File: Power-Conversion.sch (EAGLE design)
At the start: 40 parts, among them Q1 SUM90P10-19L, U7 LM2678

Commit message: Started Board Layout
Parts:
- removed U$2: SAMTEC-10, SAMTEC-10:SAMTEC-10
- added U$16: POWER_BRICK_CONNECTORS(2X6), MotherBoardParts2:POWER_BRICK_CONNECTORS(2X6)
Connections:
- net 12V: now also U$16.P$1, U$16.P$2, U$16.P$3; no longer U$2.P$1, U$2.P$2, U$2.P$3
- net 48_I_ANALOG: now also U$16.P$5
- net GND: now also U$16.P$7, U$16.P$8, U$16.P$9; no longer U$2.P$6, U$2.P$7, U$2.P$8
- net SCL: now also U$16.P$12; no longer U$2.P$5
- net SDA: now also U$16.P$6; no longer U$2.P$10
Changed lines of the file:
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@@
 <?xml version="1.0" encoding="utf-8"?>
 <!DOCTYPE eagle SYSTEM "eagle.dtd">
-<eagle version="8.3.2">
+<eagle version="8.4.1">
 <drawing>
 <settings>
@@
 <part name="SUPPLY1" library="SparkFun-PowerSymbols" deviceset="12V" device=""/>
 <part name="SUPPLY2" library="SparkFun-PowerSymbols" deviceset="12V" device=""/>
-<part name="U$2" library="SAMTEC-10" deviceset="SAMTEC-10" device=""/>
-<part name="GND5" library="supply1" deviceset="GND" device=""/>
-<part name="SUPPLY3" library="SparkFun-PowerSymbols" deviceset="12V" device=""/>
 <part name="U$17" library="MotherBoardParts2" deviceset="POWER_BRICK_CONNECTORS(2X15)" device=""/>
 <part name="U$11" library="MotherBoardParts2" deviceset="POWER_BRICK_CONNECTORS(2X15)" device=""/>
@@
 <part name="P+8" library="supply1" library_urn="urn:adsk.eagle:library:371" deviceset="VCC" device=""/>
 <part name="P+9" library="supply1" library_urn="urn:adsk.eagle:library:371" deviceset="VCC" device=""/>
+<part name="U$16" library="MotherBoardParts2" deviceset="POWER_BRICK_CONNECTORS(2X6)" device=""/>
+<part name="GND6" library="supply1" deviceset="GND" device=""/>
+<part name="SUPPLY5" library="SparkFun-PowerSymbols" deviceset="12V" device=""/>
 </parts>
 <sheets>
@@
 <instance part="SUPPLY1" gate="G$1" x="78.74" y="434.34"/>
 <instance part="SUPPLY2" gate="G$1" x="78.74" y="477.52"/>
-<instance part="U$2" gate="G$1" x="50.8" y="505.46"/>
-<instance part="GND5" gate="1" x="83.82" y="502.92"/>
-<instance part="SUPPLY3" gate="G$1" x="17.78" y="515.62"/>
 <instance part="U$17" gate="G$1" x="185.42" y="472.44"/>
 <instance part="U$11" gate="G$1" x="261.62" y="472.44"/>
@@
 <instance part="P+8" gate="VCC" x="215.9" y="391.16"/>
 <instance part="P+9" gate="VCC" x="307.34" y="391.16"/>
+<instance part="U$16" gate="G$1" x="53.34" y="508"/>
+<instance part="GND6" gate="1" x="76.2" y="502.92"/>
+<instance part="SUPPLY5" gate="G$1" x="30.48" y="515.62"/>
 </instances>
 <busses>
@@
 </segment>
 <segment>
-<pinref part="U$2" gate="G$1" pin="P$6"/>
-<wire x1="66.04" y1="515.62" x2="76.2" y2="515.62" width="0.1524" layer="91"/>
-<wire x1="76.2" y1="515.62" x2="76.2" y2="510.54" width="0.1524" layer="91"/>
-<pinref part="U$2" gate="G$1" pin="P$7"/>
-<wire x1="76.2" y1="510.54" x2="66.04" y2="510.54" width="0.1524" layer="91"/>
-<pinref part="U$2" gate="G$1" pin="P$8"/>
-<wire x1="66.04" y1="505.46" x2="76.2" y2="505.46" width="0.1524" layer="91"/>
-<wire x1="76.2" y1="505.46" x2="76.2" y2="510.54" width="0.1524" layer="91"/>
-<junction x="76.2" y="510.54"/>
-<pinref part="GND5" gate="1" pin="GND"/>
-<wire x1="76.2" y1="510.54" x2="83.82" y2="510.54" width="0.1524" layer="91"/>
-<wire x1="83.82" y1="510.54" x2="83.82" y2="505.46" width="0.1524" layer="91"/>
-</segment>
-<segment>
 <pinref part="U$8" gate="G$1" pin="P$2"/>
 <pinref part="GND4" gate="1" pin="GND"/>
@@
 <pinref part="GND9" gate="1" pin="GND"/>
 </segment>
+<segment>
+<pinref part="U$16" gate="G$1" pin="P$7"/>
+<wire x1="66.04" y1="515.62" x2="71.12" y2="515.62" width="0.1524" layer="91"/>
+<wire x1="71.12" y1="515.62" x2="71.12" y2="510.54" width="0.1524" layer="91"/>
+<pinref part="U$16" gate="G$1" pin="P$8"/>
+<wire x1="71.12" y1="510.54" x2="66.04" y2="510.54" width="0.1524" layer="91"/>
+<pinref part="U$16" gate="G$1" pin="P$9"/>
+<wire x1="66.04" y1="505.46" x2="71.12" y2="505.46" width="0.1524" layer="91"/>
+<wire x1="71.12" y1="505.46" x2="71.12" y2="510.54" width="0.1524" layer="91"/>
+<junction x="71.12" y="510.54"/>
+<wire x1="71.12" y1="510.54" x2="76.2" y2="510.54" width="0.1524" layer="91"/>
+<wire x1="76.2" y1="510.54" x2="76.2" y2="505.46" width="0.1524" layer="91"/>
+<pinref part="GND6" gate="1" pin="GND"/>
+</segment>
 </net>
 <net name="ONOFF" class="0">
@@
 <net name="12V" class="0">
 <segment>
-<pinref part="U$2" gate="G$1" pin="P$1"/>
-<wire x1="35.56" y1="515.62" x2="25.4" y2="515.62" width="0.1524" layer="91"/>
-<pinref part="U$2" gate="G$1" pin="P$2"/>
-<wire x1="35.56" y1="510.54" x2="25.4" y2="510.54" width="0.1524" layer="91"/>
-<wire x1="25.4" y1="510.54" x2="25.4" y2="515.62" width="0.1524" layer="91"/>
-<pinref part="U$2" gate="G$1" pin="P$3"/>
-<wire x1="35.56" y1="505.46" x2="25.4" y2="505.46" width="0.1524" layer="91"/>
-<wire x1="25.4" y1="505.46" x2="25.4" y2="510.54" width="0.1524" layer="91"/>
-<junction x="25.4" y="510.54"/>
-<label x="25.4" y="515.62" size="1.778" layer="95"/>
-<pinref part="SUPPLY3" gate="G$1" pin="12V"/>
-<wire x1="25.4" y1="510.54" x2="17.78" y2="510.54" width="0.1524" layer="91"/>
-<wire x1="17.78" y1="510.54" x2="17.78" y2="515.62" width="0.1524" layer="91"/>
-</segment>
-<segment>
 <pinref part="U$8" gate="G$1" pin="P$1"/>
 <pinref part="SUPPLY2" gate="G$1" pin="12V"/>
@@
 <wire x1="78.74" y1="426.72" x2="78.74" y2="434.34" width="0.1524" layer="91"/>
 </segment>
+<segment>
+<pinref part="U$16" gate="G$1" pin="P$1"/>
+<wire x1="40.64" y1="515.62" x2="35.56" y2="515.62" width="0.1524" layer="91"/>
+<pinref part="U$16" gate="G$1" pin="P$2"/>
+<wire x1="35.56" y1="515.62" x2="35.56" y2="510.54" width="0.1524" layer="91"/>
+<wire x1="35.56" y1="510.54" x2="40.64" y2="510.54" width="0.1524" layer="91"/>
+<pinref part="U$16" gate="G$1" pin="P$3"/>
+<wire x1="40.64" y1="505.46" x2="35.56" y2="505.46" width="0.1524" layer="91"/>
+<wire x1="35.56" y1="505.46" x2="35.56" y2="510.54" width="0.1524" layer="91"/>
+<junction x="35.56" y="510.54"/>
+<wire x1="35.56" y1="510.54" x2="30.48" y2="510.54" width="0.1524" layer="91"/>
+<wire x1="30.48" y1="510.54" x2="30.48" y2="515.62" width="0.1524" layer="91"/>
+<pinref part="SUPPLY5" gate="G$1" pin="12V"/>
+</segment>
 </net>
 <net name="SCL" class="0">
-<segment>
-<pinref part="U$2" gate="G$1" pin="P$5"/>
-<wire x1="35.56" y1="495.3" x2="25.4" y2="495.3" width="0.1524" layer="91"/>
-<label x="25.4" y="495.3" size="1.778" layer="95"/>
-</segment>
 <segment>
 <pinref part="U$13" gate="G$1" pin="P$12"/>
@@
 <label x="342.9" y="345.44" size="1.778" layer="95"/>
 </segment>
+<segment>
+<pinref part="U$16" gate="G$1" pin="P$12"/>
+<wire x1="66.04" y1="490.22" x2="76.2" y2="490.22" width="0.1524" layer="91"/>
+<label x="71.12" y="490.22" size="1.778" layer="95"/>
+</segment>
 </net>
 <net name="SDA" class="0">
-<segment>
-<pinref part="U$2" gate="G$1" pin="P$10"/>
-<wire x1="66.04" y1="495.3" x2="76.2" y2="495.3" width="0.1524" layer="91"/>
-<label x="71.12" y="495.3" size="1.778" layer="95"/>
-</segment>
 <segment>
 <pinref part="U$13" gate="G$1" pin="P$6"/>
@@
 <wire x1="312.42" y1="345.44" x2="304.8" y2="345.44" width="0.1524" layer="91"/>
 <label x="304.8" y="345.44" size="1.778" layer="95"/>
+</segment>
+<segment>
+<pinref part="U$16" gate="G$1" pin="P$6"/>
+<wire x1="40.64" y1="490.22" x2="30.48" y2="490.22" width="0.1524" layer="91"/>
+<label x="30.48" y="490.22" size="1.778" layer="95"/>
 </segment>
 </net>
@@
 <label x="175.26" y="111.76" size="1.778" layer="95"/>
 </segment>
-</net>
+<segment>
+<pinref part="U$16" gate="G$1" pin="P$5"/>
+<wire x1="40.64" y1="495.3" x2="22.86" y2="495.3" width="0.1524" layer="91"/>
+<label x="22.86" y="495.3" size="1.778" layer="95"/>
+</segment>
+</net>

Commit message: Fix Board Layout
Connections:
- removed net +48_RAW: J1.1
- removed net 48_GND: J2.1
- net +48V_RAW: now also J1.1
- net 48V_GND: now also J2.1
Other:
- moved on the sheet: R3
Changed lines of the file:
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@@
 <instance part="P+3" gate="1" x="228.6" y="187.96"/>
 <instance part="P+4" gate="1" x="238.76" y="187.96"/>
-<instance part="R3" gate="G$1" x="119.38" y="175.26" rot="R90">
-<attribute name="PARTNO" value="1.00MHCT-ND" x="119.38" y="175.26" size="0.0254" layer="96" font="vector" display="off"/>
-<attribute name="BOM" value="INCLUDE" x="119.38" y="175.26" size="0.0254" layer="96" font="vector" display="off"/>
+<instance part="R3" gate="G$1" x="119.38" y="172.72" rot="R90">
+<attribute name="PARTNO" value="1.00MHCT-ND" x="119.38" y="172.72" size="0.0254" layer="96" font="vector" display="off"/>
+<attribute name="BOM" value="INCLUDE" x="119.38" y="172.72" size="0.0254" layer="96" font="vector" display="off"/>
 </instance>
 <instance part="D1" gate="G$1" x="129.54" y="187.96" smashed="yes" rot="R90">
@@
 <segment>
 <pinref part="R3" gate="G$1" pin="1"/>
-<wire x1="119.38" y1="170.18" x2="119.38" y2="157.48" width="0.1524" layer="91"/>
+<wire x1="119.38" y1="167.64" x2="119.38" y2="157.48" width="0.1524" layer="91"/>
 <label x="119.38" y="157.48" size="1.778" layer="95"/>
 </segment>
@@
 <pinref part="P-6" gate="1" pin="V-"/>
 <label x="292.1" y="360.68" size="1.778" layer="95"/>
+</segment>
+<segment>
+<pinref part="J2" gate="G$1" pin="1"/>
+<wire x1="30.48" y1="99.06" x2="20.32" y2="99.06" width="0.1524" layer="91"/>
+<label x="20.32" y="99.06" size="1.778" layer="95"/>
 </segment>
 </net>
@@
 <pinref part="R3" gate="G$1" pin="2"/>
 <pinref part="D1" gate="G$1" pin="A"/>
-<wire x1="119.38" y1="182.88" x2="119.38" y2="180.34" width="0.1524" layer="91"/>
+<wire x1="119.38" y1="182.88" x2="119.38" y2="177.8" width="0.1524" layer="91"/>
 <wire x1="129.54" y1="185.42" x2="129.54" y2="182.88" width="0.1524" layer="91"/>
 <wire x1="129.54" y1="182.88" x2="119.38" y2="182.88" width="0.1524" layer="91"/>
@@
 <wire x1="106.68" y1="203.2" x2="99.06" y2="203.2" width="0.1524" layer="91"/>
 <label x="99.06" y="203.2" size="1.778" layer="95"/>
+</segment>
+<segment>
+<pinref part="J1" gate="G$1" pin="1"/>
+<wire x1="30.48" y1="104.14" x2="20.32" y2="104.14" width="0.1524" layer="91"/>
+<label x="20.32" y="104.14" size="1.778" layer="95"/>
 </segment>
 </net>
@@
 </segment>
 </net>
-<net name="+48_RAW" class="0">
-<segment>
-<pinref part="J1" gate="G$1" pin="1"/>
-<wire x1="30.48" y1="104.14" x2="20.32" y2="104.14" width="0.1524" layer="91"/>
-<label x="20.32" y="104.14" size="1.778" layer="95"/>
-</segment>
-</net>
-<net name="48_GND" class="0">
-<segment>
-<pinref part="J2" gate="G$1" pin="1"/>
-<wire x1="30.48" y1="99.06" x2="20.32" y2="99.06" width="0.1524" layer="91"/>
-<label x="20.32" y="99.06" size="1.778" layer="95"/>
-</segment>
-</net>

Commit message: Routed Board
Added Diodes
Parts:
- added U$18, U$19, U$2: DIODE, diode:DIODE
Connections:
- removed net +48_SNS: U$1.IP-@3, U$1.IP-@4
- removed net VCC: U$13.P$1, U$13.P$2, U$13.P$7, U$13.P$8, U$14.P$1, U$14.P$2, U$14.P$7, U$14.P$8, U$15.P$1, U$15.P$2, U$15.P$7, U$15.P$8
- new net +12V_1: U$17.P$1, U$17.P$16, U$17.P$17, U$17.P$18, U$17.P$19, U$17.P$2, U$17.P$20, U$17.P$21, U$17.P$22, U$17.P$3, U$17.P$4, U$17.P$5, U$17.P$6, U$17.P$7, U$2.IN2
- new net +12V_2: U$11.P$1, U$11.P$16, U$11.P$17, U$11.P$18, U$11.P$19, U$11.P$2, U$11.P$20, U$11.P$21, U$11.P$22, U$11.P$3, U$11.P$4, U$11.P$5, U$11.P$6, U$11.P$7, U$18.IN2
- new net +12V_3: U$12.P$1, U$12.P$16, U$12.P$17, U$12.P$18, U$12.P$19, U$12.P$2, U$12.P$20, U$12.P$21, U$12.P$22, U$12.P$3, U$12.P$4, U$12.P$5, U$12.P$6, U$12.P$7, U$19.IN2
- new net +48V_SNS: U$1.IP-@3, U$1.IP-@4, U$13.P$1, U$13.P$2, U$13.P$7, U$13.P$8, U$14.P$1, U$14.P$2, U$14.P$7, U$14.P$8, U$15.P$1, U$15.P$2, U$15.P$7, U$15.P$8
- net +12V: now also U$18.OUT, U$19.OUT, U$2.OUT; no longer U$11.P$1, U$11.P$16, U$11.P$17, U$11.P$18, U$11.P$19, U$11.P$2, U$11.P$20, U$11.P$21, U$11.P$22, U$11.P$3, U$11.P$4, U$11.P$5, U$11.P$6, U$11.P$7, U$12.P$1, U$12.P$16, U$12.P$17, U$12.P$18, U$12.P$19, U$12.P$2, U$12.P$20, U$12.P$21, U$12.P$22, U$12.P$3, U$12.P$4, U$12.P$5, U$12.P$6, U$12.P$7, U$17.P$1, U$17.P$16, U$17.P$17, U$17.P$18, U$17.P$19, U$17.P$2, U$17.P$20, U$17.P$21, U$17.P$22, U$17.P$3, U$17.P$4, U$17.P$5, U$17.P$6, U$17.P$7
- net 12V: now also U$8.P$2; no longer U$3.P$2
- net GND: now also U$3.P$2; no longer U$8.P$2

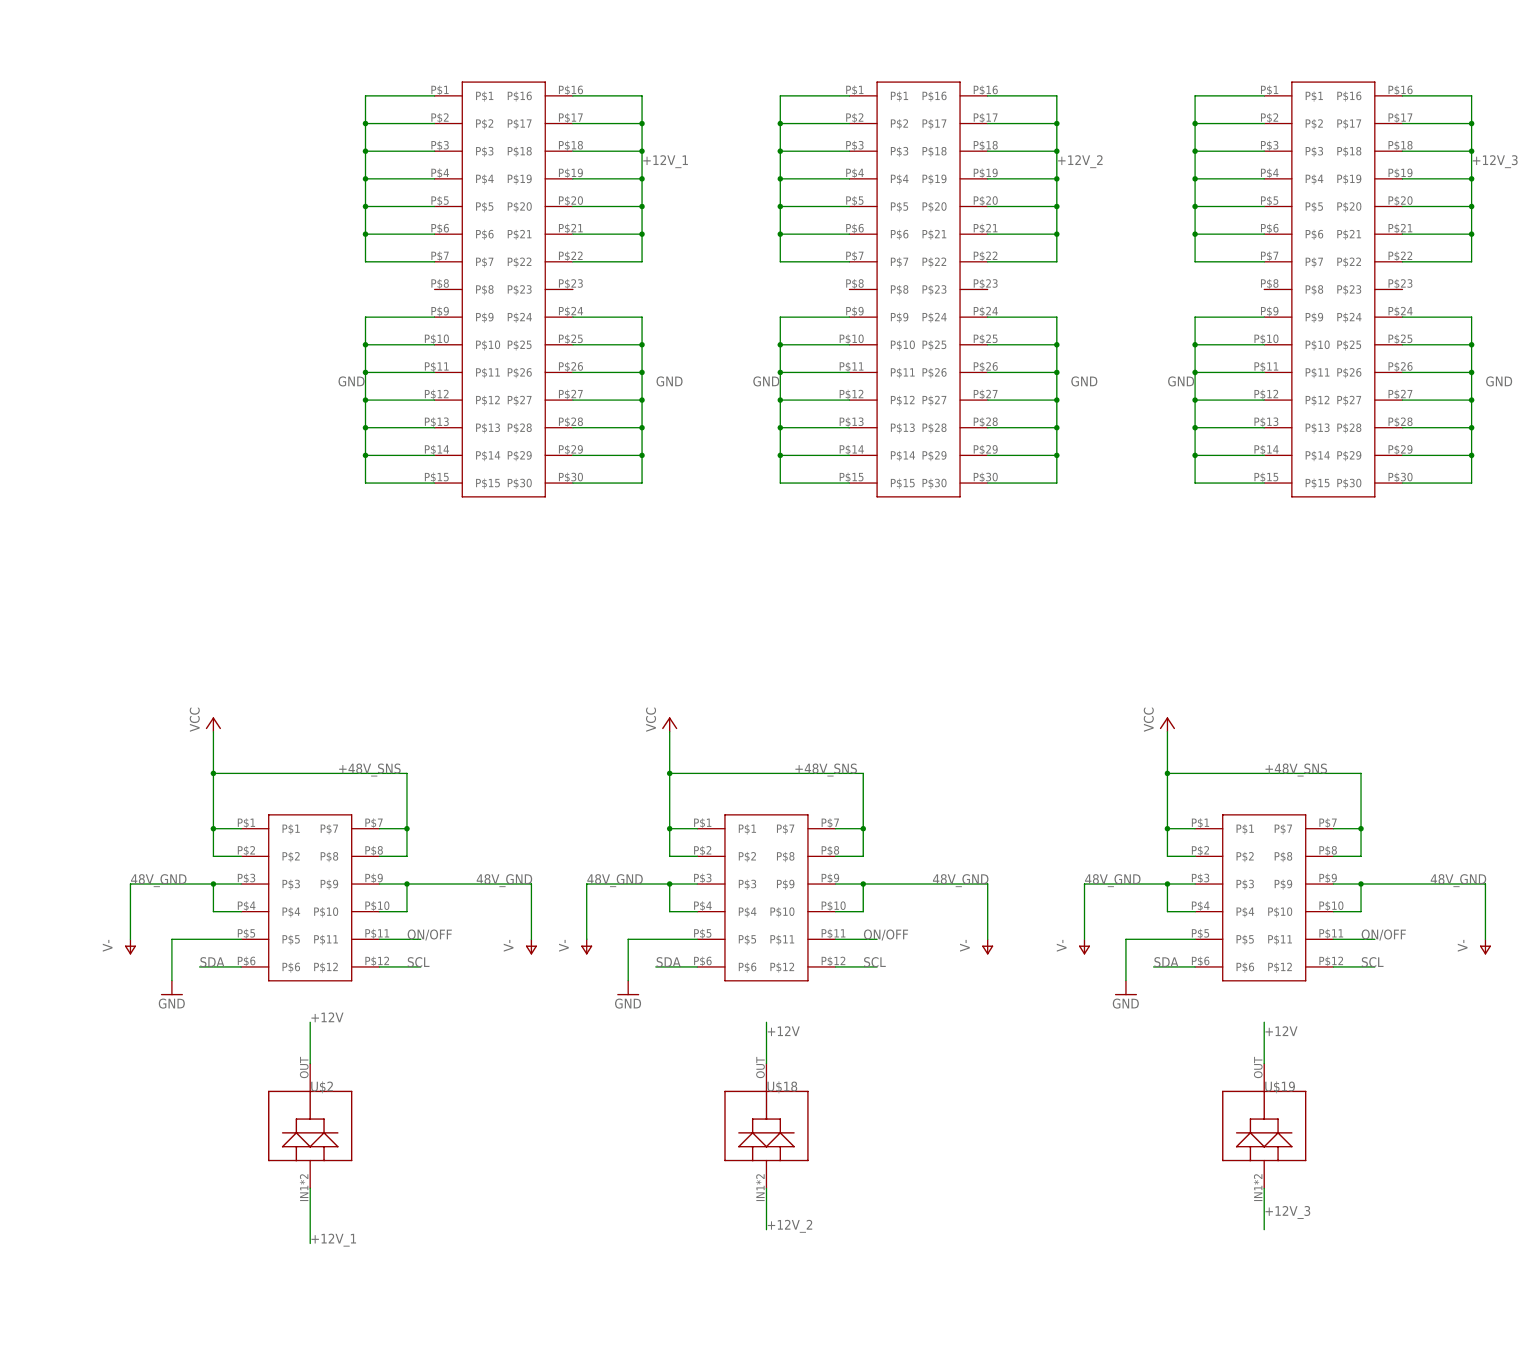
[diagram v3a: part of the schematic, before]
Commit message: Added new connectors for 8th bricks
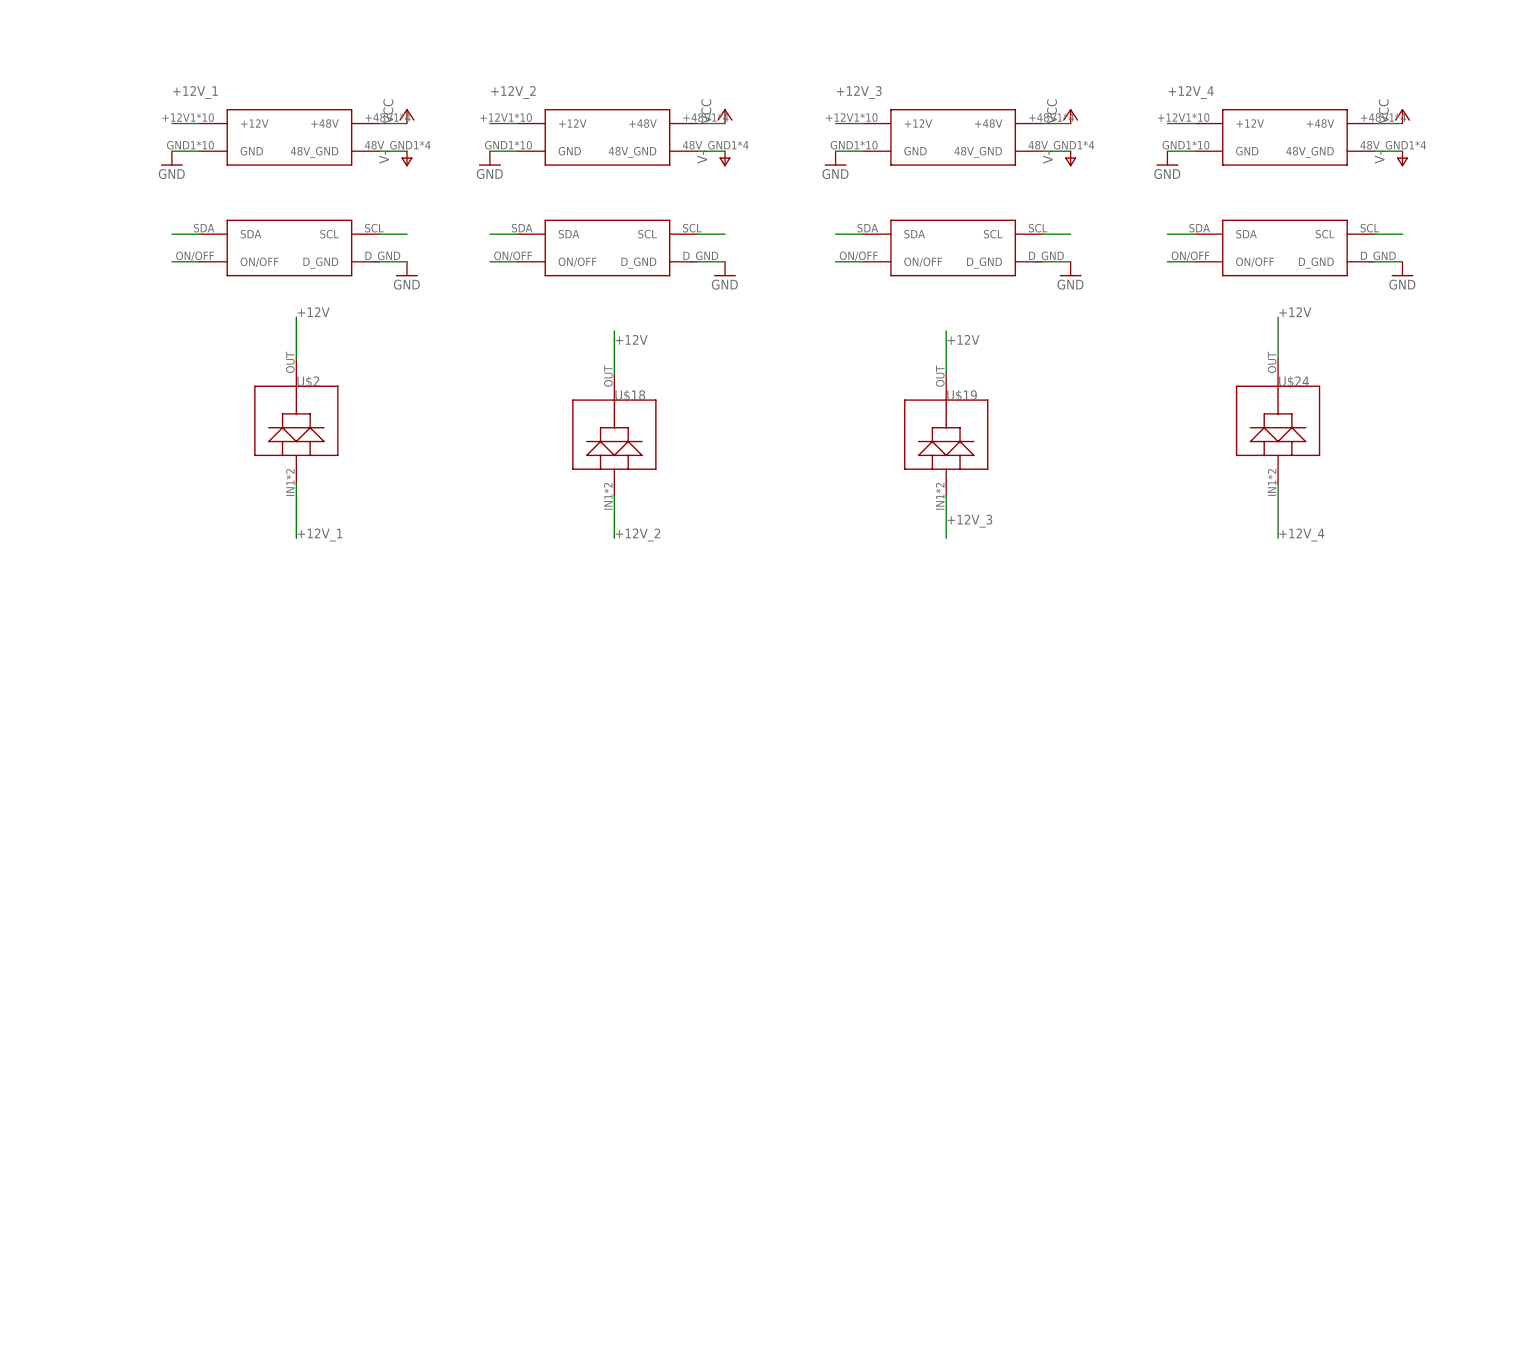
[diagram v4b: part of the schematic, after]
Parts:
- removed U$11, U$12, U$17: POWER_BRICK_CONNECTORS(2X15), MotherBoardParts2:POWER_BRICK_CONNECTORS(2X15)
- removed U$13, U$14, U$15: POWER_BRICK_CONNECTORS(2X6), MotherBoardParts2:POWER_BRICK_CONNECTORS(2X6)
- added U$20, U$21, U$22, U$23: BRICK_TO_POWER_DIST_WHOLE, MotherBoardParts2:BRICK_TO_POWER_DIST_WHOLE
- added U$24: DIODE, diode:DIODE
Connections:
- new net +12V_4: U$23.+12V, U$24.IN2
- new net V-: U$20.48V_GND, U$21.48V_GND, U$22.48V_GND, U$23.48V_GND
- new net VCC: U$20.+48V, U$21.+48V, U$22.+48V, U$23.+48V
- net +12V: now also U$24.OUT
- net +12V_1: now also U$20.+12V; no longer U$17.P$1, U$17.P$16, U$17.P$17, U$17.P$18, U$17.P$19, U$17.P$2, U$17.P$20, U$17.P$21, U$17.P$22, U$17.P$3, U$17.P$4, U$17.P$5, U$17.P$6, U$17.P$7
- net +12V_2: now also U$21.+12V; no longer U$11.P$1, U$11.P$16, U$11.P$17, U$11.P$18, U$11.P$19, U$11.P$2, U$11.P$20, U$11.P$21, U$11.P$22, U$11.P$3, U$11.P$4, U$11.P$5, U$11.P$6, U$11.P$7
- net +12V_3: now also U$22.+12V; no longer U$12.P$1, U$12.P$16, U$12.P$17, U$12.P$18, U$12.P$19, U$12.P$2, U$12.P$20, U$12.P$21, U$12.P$22, U$12.P$3, U$12.P$4, U$12.P$5, U$12.P$6, U$12.P$7
- net +48V_SNS: no longer U$13.P$1, U$13.P$2, U$13.P$7, U$13.P$8, U$14.P$1, U$14.P$2, U$14.P$7, U$14.P$8, U$15.P$1, U$15.P$2, U$15.P$7, U$15.P$8
- net 48V_GND: no longer U$13.P$10, U$13.P$3, U$13.P$4, U$13.P$9, U$14.P$10, U$14.P$3, U$14.P$4, U$14.P$9, U$15.P$10, U$15.P$3, U$15.P$4, U$15.P$9
- net GND: now also U$20.D_GND, U$20.GND, U$21.D_GND, U$21.GND, U$22.D_GND, U$22.GND, U$23.D_GND, U$23.GND; no longer U$11.P$10, U$11.P$11, U$11.P$12, U$11.P$13, U$11.P$14, U$11.P$15, U$11.P$24, U$11.P$25, U$11.P$26, U$11.P$27, U$11.P$28, U$11.P$29, U$11.P$30, U$11.P$9, U$12.P$10, U$12.P$11, U$12.P$12, U$12.P$13, U$12.P$14, U$12.P$15, U$12.P$24, U$12.P$25, U$12.P$26, U$12.P$27, U$12.P$28, U$12.P$29, U$12.P$30, U$12.P$9, U$13.P$5, U$14.P$5, U$15.P$5, U$17.P$10, U$17.P$11, U$17.P$12, U$17.P$13, U$17.P$14, U$17.P$15, U$17.P$24, U$17.P$25, U$17.P$26, U$17.P$27, U$17.P$28, U$17.P$29, U$17.P$30, U$17.P$9
- net ON/OFF: now also U$20.ON/OFF, U$21.ON/OFF, U$22.ON/OFF, U$23.ON/OFF; no longer U$13.P$11, U$14.P$11, U$15.P$11
- net SCL: now also U$20.SCL, U$21.SCL, U$22.SCL, U$23.SCL; no longer U$13.P$12, U$14.P$12, U$15.P$12
- net SDA: now also U$20.SDA, U$21.SDA, U$22.SDA, U$23.SDA; no longer U$13.P$6, U$14.P$6, U$15.P$6
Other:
- moved on the sheet: U$18, U$19, U$2
